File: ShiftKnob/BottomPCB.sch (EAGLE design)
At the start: 38 parts, among them IC2 UA78M05DCY, J1 AVR_SPI_PRG_6PTH, Q1 16MHz, Q2 MOSFET-NCHANNELSMD, Q3 MOSFET-PCHANNELSMD, Q4 MOSFET-NCHANNELSMD, Q5 MOSFET-NCHANNELSMD, Q6 MOSFET-NCHANNELSMD, U1 ATMEGA328, U3 FT232RL-BASICSSOP

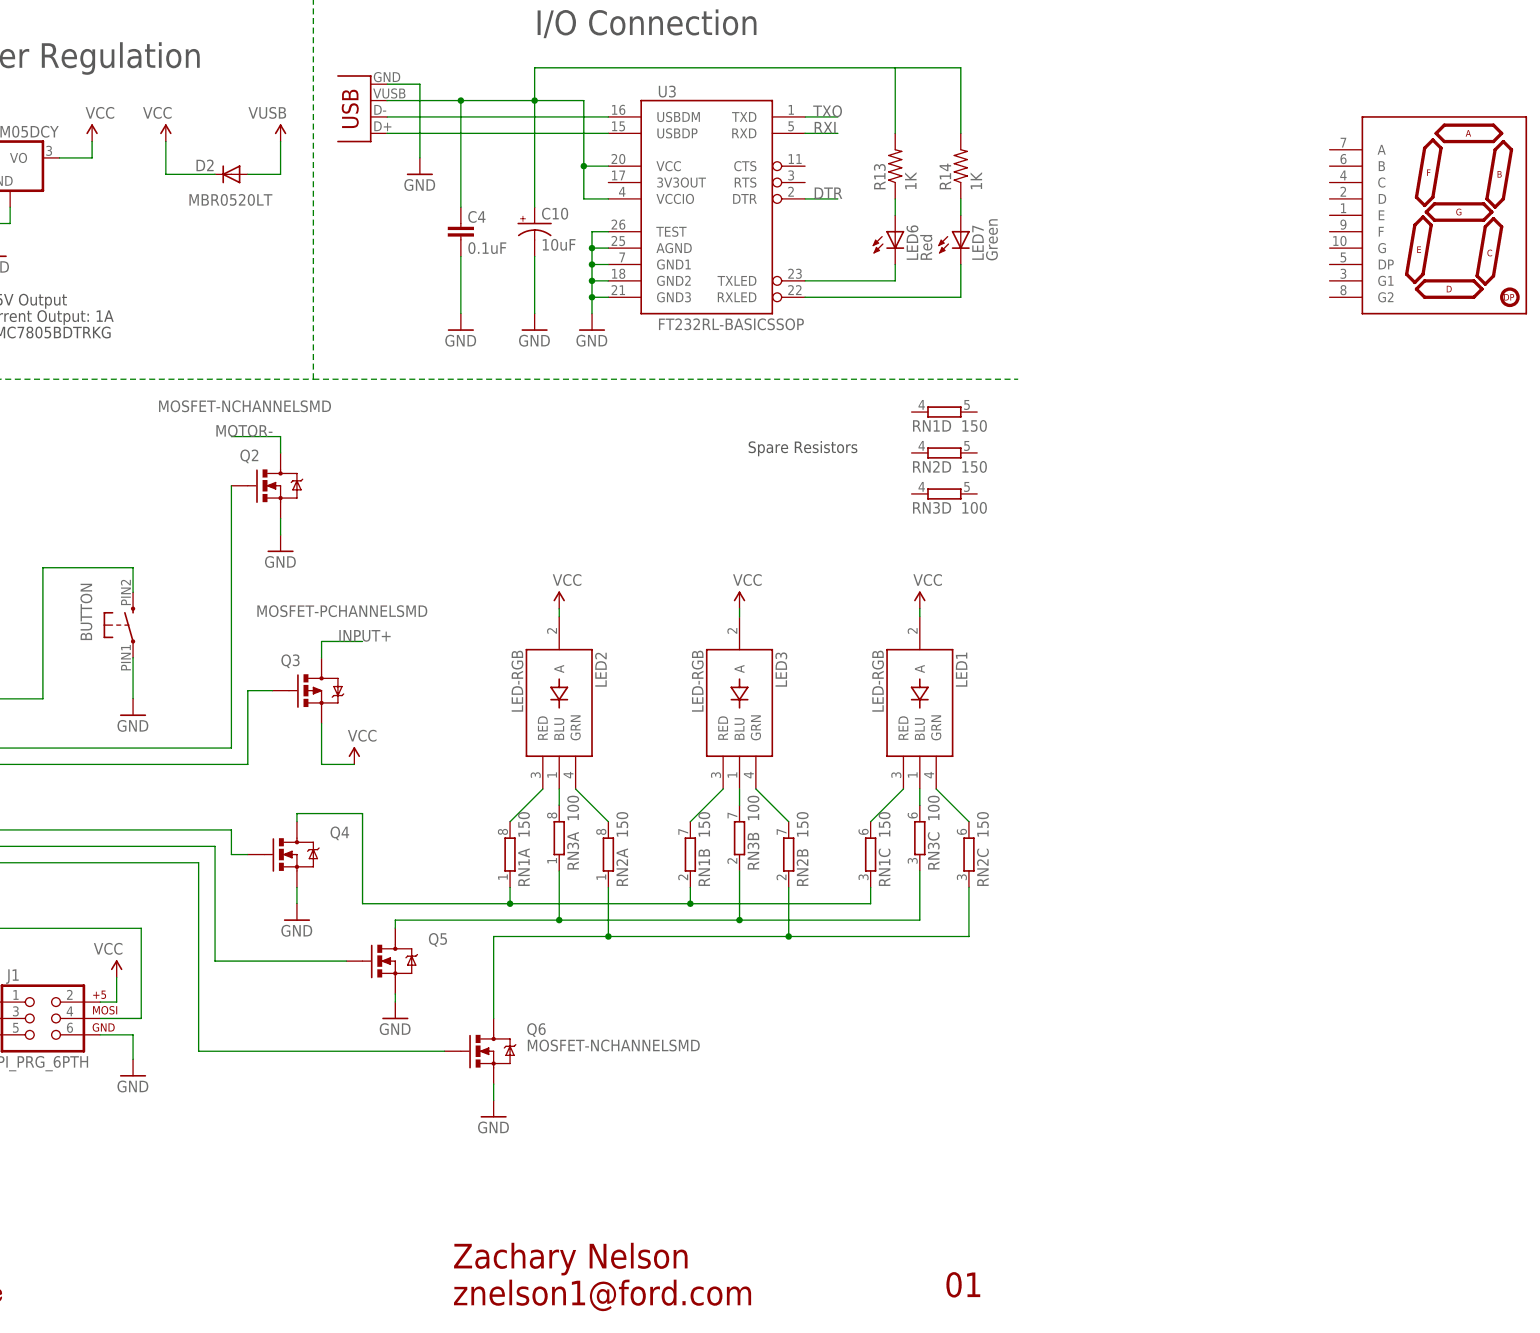
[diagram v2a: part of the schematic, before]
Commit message: swap out button for edge_mount button in Ford_frames library.
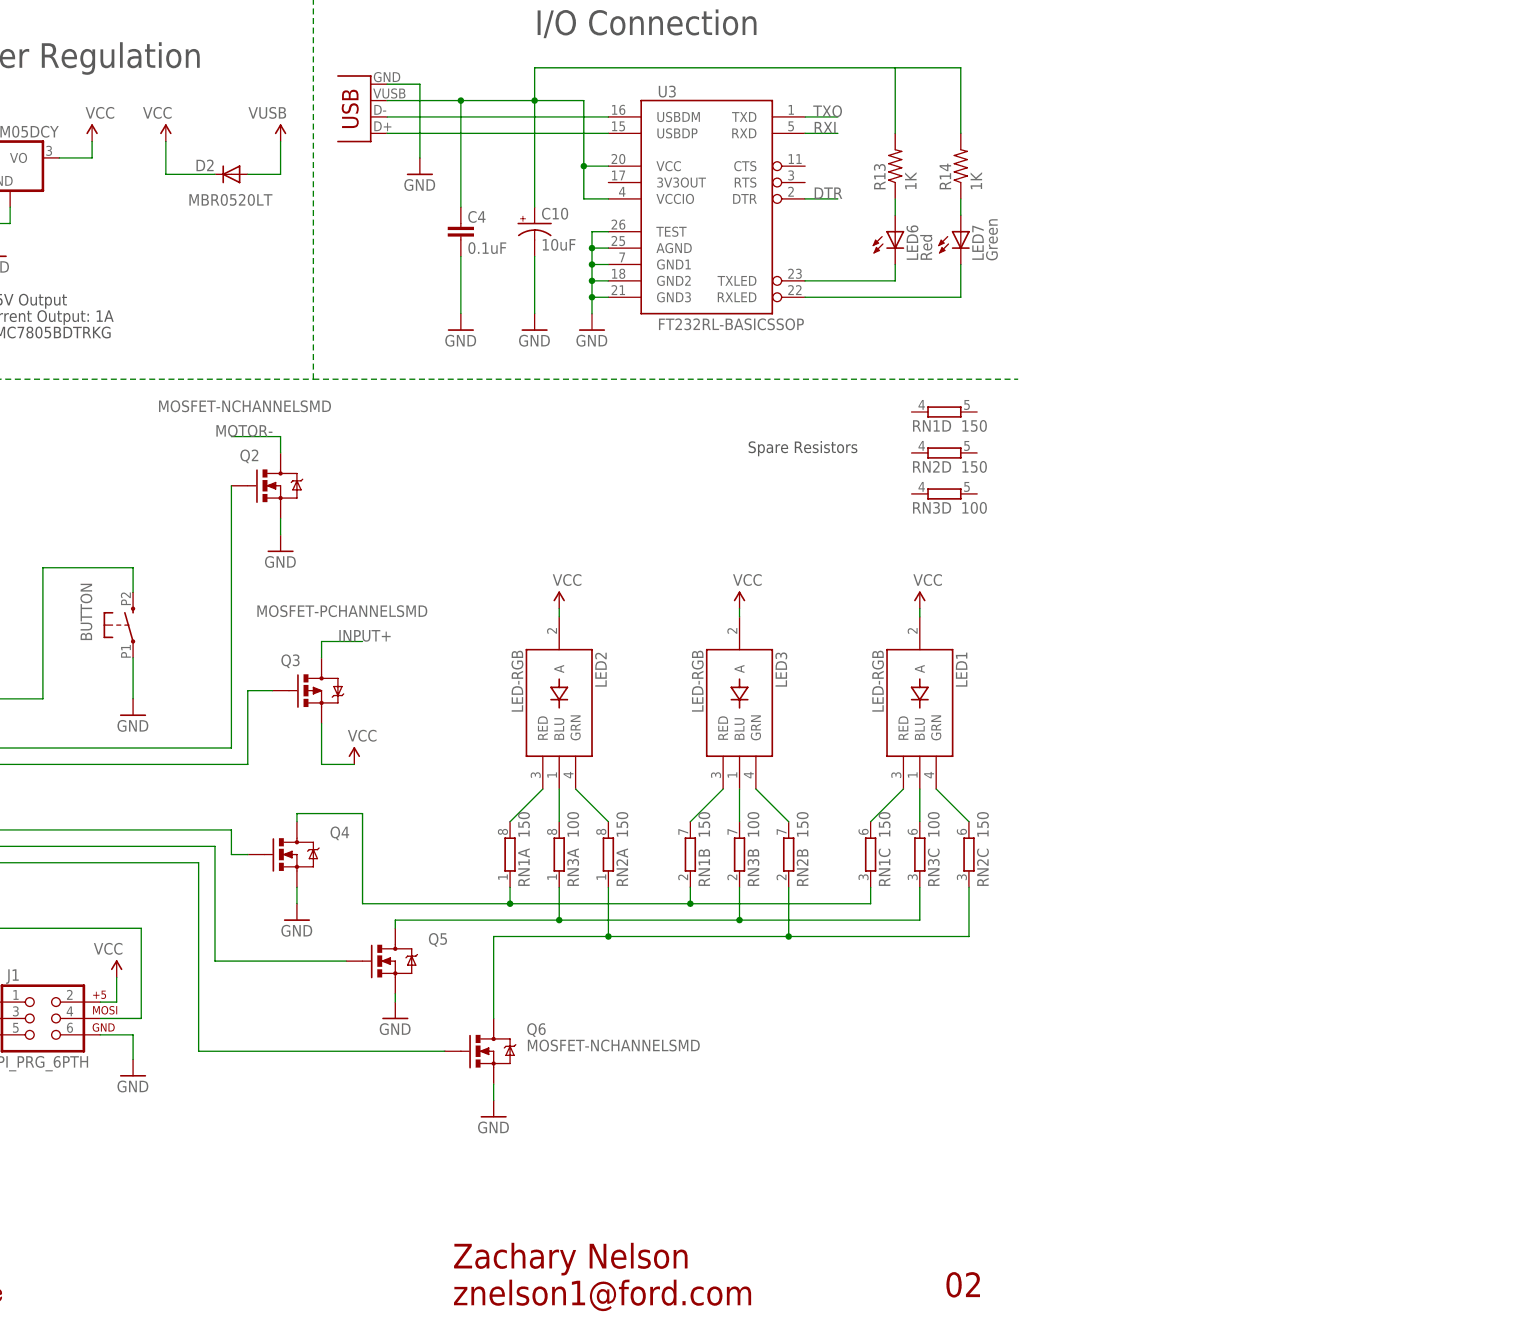
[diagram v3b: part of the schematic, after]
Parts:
- removed U$2: 7-SEGMENT-DISPLAY-1"-RED, SparkFun-Displays:7-SEGMENT-DISPLAY-1"-RED
- BUTTON: value BUTTON_RIGHTANGLE_SMD -> BUTTON_EDGE; device FORD_frames:BUTTON_RIGHTANGLE_SMD -> FORD_frames:BUTTON_EDGE
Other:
- note added: "02"
- note removed: "01"
- moved on the sheet: RN3A, RN3B, RN3C
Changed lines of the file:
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@@
 <part name="P+4" library="SparkFun" deviceset="3.3V" device="" value="VCC"/>
 <part name="P+5" library="SparkFun" deviceset="3.3V" device="" value="VCC"/>
-<part name="BUTTON" library="FORD_frames" deviceset="BUTTON_RIGHTANGLE_SMD" device=""/>
-<part name="U$2" library="SparkFun-Displays" deviceset="7-SEGMENT-DISPLAY-1&quot;-RED" device=""/>
+<part name="BUTTON" library="FORD_frames" deviceset="BUTTON_EDGE" device=""/>
 <part name="UPPER" library="SparkFun-Connectors" deviceset="M04" device="PTH"/>
 <part name="LOWER" library="SparkFun-Connectors" deviceset="M04" device="PTH"/>
@@
 <sheet>
 <plain>
-<text x="264.16" y="8.89" size="3.81" layer="94">01</text>
+<text x="264.16" y="8.89" size="3.81" layer="94">02</text>
 <text x="187.96" y="7.62" size="3.81" layer="94">Zachary Nelson
 znelson1@ford.com</text>
@@
 <instance part="RN2" gate="C" x="267.97" y="77.47" rot="R90"/>
 <instance part="RN2" gate="D" x="264.16" y="139.7"/>
-<instance part="RN3" gate="A" x="204.47" y="80.01" rot="R90"/>
-<instance part="RN3" gate="B" x="232.41" y="80.01" rot="R90"/>
-<instance part="RN3" gate="C" x="260.35" y="80.01" rot="R90"/>
+<instance part="RN3" gate="A" x="204.47" y="77.47" rot="R90"/>
+<instance part="RN3" gate="B" x="232.41" y="77.47" rot="R90"/>
+<instance part="RN3" gate="C" x="260.35" y="77.47" rot="R90"/>
 <instance part="RN3" gate="D" x="264.16" y="133.35"/>
 <instance part="C4" gate="G$1" x="189.23" y="175.26" smashed="yes" rot="R180">
@@
 <attribute name="NAME" x="132.08" y="110.49" size="1.778" layer="95" rot="R90"/>
 </instance>
-<instance part="U$2" gate="G$1" x="344.17" y="176.53"/>
 <instance part="UPPER" gate="G$1" x="15.24" y="180.34"/>
 <instance part="LOWER" gate="G$1" x="15.24" y="160.02"/>
@@
 <segment>
 <label x="101.6" y="78.74" size="1.778" layer="95"/>
-<wire x1="204.47" y1="67.31" x2="204.47" y2="74.93" width="0.1524" layer="91"/>
+<wire x1="204.47" y1="67.31" x2="204.47" y2="72.39" width="0.1524" layer="91"/>
 <wire x1="204.47" y1="67.31" x2="232.41" y2="67.31" width="0.1524" layer="91"/>
-<wire x1="232.41" y1="67.31" x2="232.41" y2="74.93" width="0.1524" layer="91"/>
-<wire x1="260.35" y1="67.31" x2="260.35" y2="74.93" width="0.1524" layer="91"/>
+<wire x1="232.41" y1="67.31" x2="232.41" y2="72.39" width="0.1524" layer="91"/>
+<wire x1="260.35" y1="67.31" x2="260.35" y2="72.39" width="0.1524" layer="91"/>
 <wire x1="232.41" y1="67.31" x2="260.35" y2="67.31" width="0.1524" layer="91"/>
 <junction x="232.41" y="67.31"/>
@@
 <segment>
 <pinref part="LED3" gate="G$1" pin="BLU"/>
-<wire x1="232.41" y1="85.09" x2="232.41" y2="87.63" width="0.1524" layer="91"/>
+<wire x1="232.41" y1="82.55" x2="232.41" y2="87.63" width="0.1524" layer="91"/>
 <pinref part="RN3" gate="B" pin="2"/>
 </segment>
@@
 <segment>
 <pinref part="LED2" gate="G$1" pin="BLU"/>
-<wire x1="204.47" y1="87.63" x2="204.47" y2="85.09" width="0.1524" layer="91"/>
+<wire x1="204.47" y1="87.63" x2="204.47" y2="82.55" width="0.1524" layer="91"/>
 <pinref part="RN3" gate="A" pin="2"/>
 </segment>
@@
 <segment>
 <pinref part="LED1" gate="G$1" pin="BLU"/>
-<wire x1="260.35" y1="85.09" x2="260.35" y2="87.63" width="0.1524" layer="91"/>
+<wire x1="260.35" y1="82.55" x2="260.35" y2="87.63" width="0.1524" layer="91"/>
 <pinref part="RN3" gate="C" pin="2"/>
 </segment>

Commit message: everything on the board. need to route traces.
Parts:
- R13, R14: value 1K -> 10K
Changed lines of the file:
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@@
 <part name="U$6" library="FORD_frames" deviceset="USB-MINI-B_VERTICAL" device=""/>
 <part name="GND20" library="SparkFun" deviceset="GND" device=""/>
-<part name="R13" library="SparkFun" deviceset="RESISTOR" device="0402-RES" value="1K"/>
-<part name="R14" library="SparkFun" deviceset="RESISTOR" device="0402-RES" value="1K"/>
+<part name="R13" library="SparkFun" deviceset="RESISTOR" device="0402-RES" value="10K"/>
+<part name="R14" library="SparkFun" deviceset="RESISTOR" device="0402-RES" value="10K"/>
 <part name="LED6" library="SparkFun" deviceset="LED" device="0603" value="Red"/>
 <part name="LED7" library="SparkFun" deviceset="LED" device="0603" value="Green"/>

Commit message: fix VCC connection on RGB LEDs. Connection was not previously made between pin2 and VCC on each LED.
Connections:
- removed net 3.3V: LED1.A, LED2.A, LED3.A
- net VCC: now also LED1.A, LED2.A, LED3.A
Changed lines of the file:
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@@
 <label x="25.4" y="185.42" size="1.778" layer="95"/>
+</segment>
+<segment>
+<pinref part="LED2" gate="G$1" pin="A"/>
+<wire x1="204.47" y1="115.57" x2="204.47" y2="114.3" width="0.1524" layer="91"/>
+<pinref part="P+3" gate="G$1" pin="3.3V"/>
+</segment>
+<segment>
+<pinref part="LED3" gate="G$1" pin="A"/>
+<wire x1="232.41" y1="115.57" x2="232.41" y2="114.3" width="0.1524" layer="91"/>
+<pinref part="P+4" gate="G$1" pin="3.3V"/>
+</segment>
+<segment>
+<pinref part="LED1" gate="G$1" pin="A"/>
+<wire x1="260.35" y1="115.57" x2="260.35" y2="114.3" width="0.1524" layer="91"/>
+<pinref part="P+5" gate="G$1" pin="3.3V"/>
 </segment>
 </net>
@@
 </segment>
 </net>
-<net name="3.3V" class="0">
-<segment>
-<pinref part="LED2" gate="G$1" pin="A"/>
-<wire x1="204.47" y1="115.57" x2="204.47" y2="114.3" width="0.1524" layer="91"/>
-<pinref part="P+3" gate="G$1" pin="3.3V"/>
-</segment>
-<segment>
-<pinref part="LED3" gate="G$1" pin="A"/>
-<wire x1="232.41" y1="115.57" x2="232.41" y2="114.3" width="0.1524" layer="91"/>
-<pinref part="P+4" gate="G$1" pin="3.3V"/>
-</segment>
-<segment>
-<pinref part="LED1" gate="G$1" pin="A"/>
-<wire x1="260.35" y1="115.57" x2="260.35" y2="114.3" width="0.1524" layer="91"/>
-<pinref part="P+5" gate="G$1" pin="3.3V"/>
-</segment>
-</net>

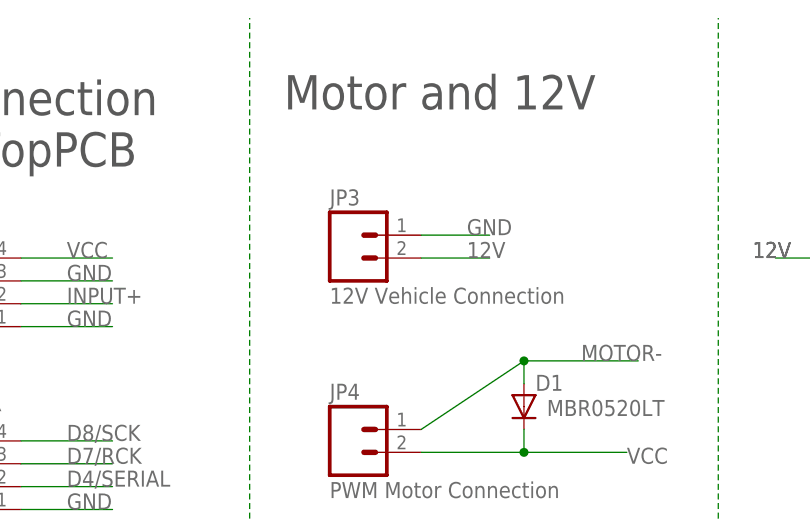
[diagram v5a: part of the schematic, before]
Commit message: change 12V connection to 2 through hole solder points.
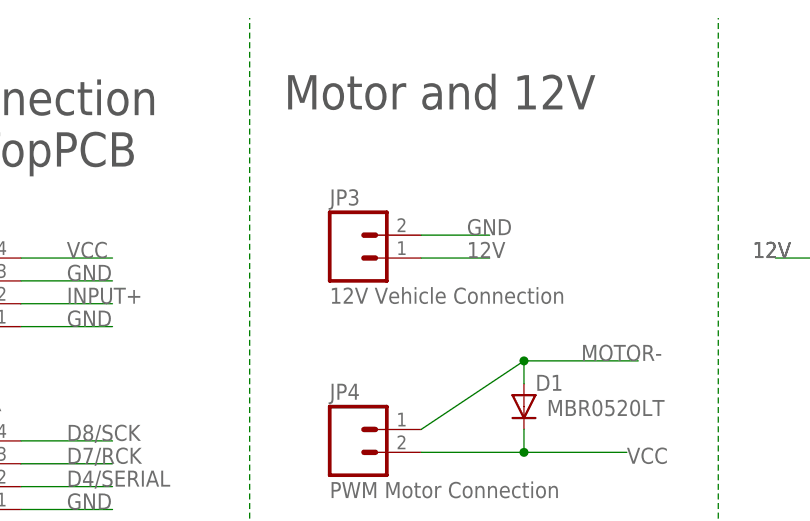
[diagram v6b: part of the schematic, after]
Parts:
- JP3: device SparkFun-Connectors:M02-JST-2MM-SMT -> SparkFun-Connectors:M02PTH; PROD_ID CONN-08352 -> (none)
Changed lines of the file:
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@@
 <part name="C2" library="SparkFun" deviceset="CAP" device="0402-CAP" value="0.1uF"/>
 <part name="U$3" library="SparkFun" deviceset="OSHW-LOGO" device="S"/>
-<part name="JP3" library="SparkFun-Connectors" deviceset="M02" device="-JST-2MM-SMT" value="12V Vehicle Connection">
-<attribute name="PROD_ID" value="CONN-08352"/>
-</part>
+<part name="JP3" library="SparkFun-Connectors" deviceset="M02" device="PTH" value="12V Vehicle Connection"/>
 <part name="LED2" library="FORD_frames" deviceset="LED-RGB" device=""/>
 <part name="LED3" library="FORD_frames" deviceset="LED-RGB" device=""/>

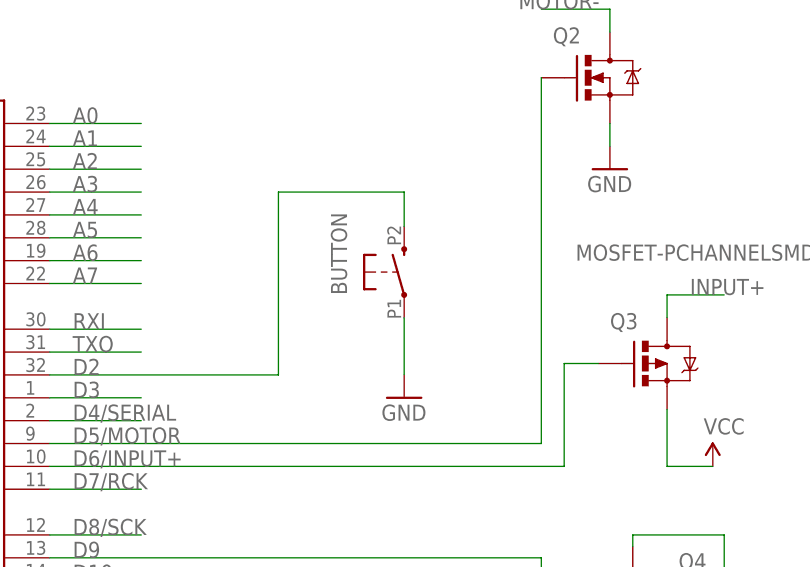
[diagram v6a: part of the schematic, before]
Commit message: swap pins on button for easier board layout.
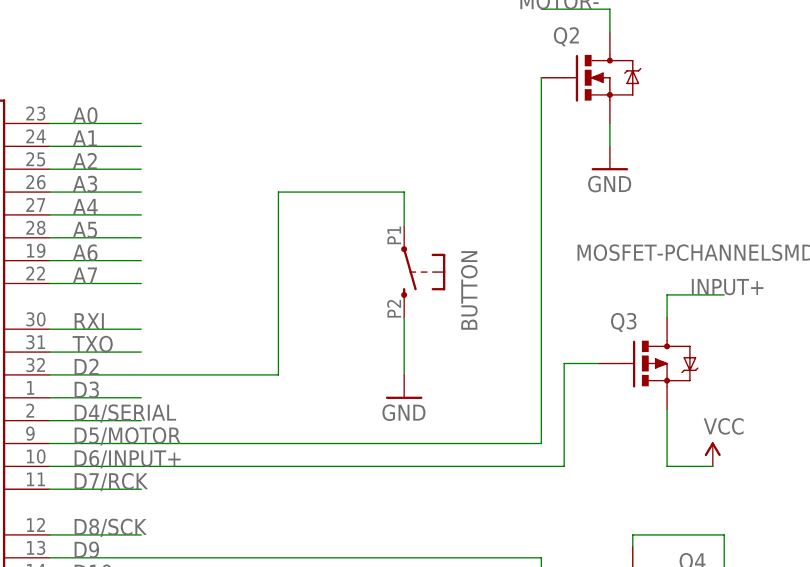
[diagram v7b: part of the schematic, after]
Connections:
- net D2: now also BUTTON.1; no longer BUTTON.2
- net GND: now also BUTTON.2; no longer BUTTON.1
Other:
- moved on the sheet: BUTTON
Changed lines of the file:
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@@
 <setting verticaltext="up"/>
 </settings>
-<grid distance="0.1" unitdist="inch" unit="inch" style="lines" multiple="1" display="no" altdistance="0.01" altunitdist="inch" altunit="inch"/>
+<grid distance="0.05" unitdist="inch" unit="inch" style="lines" multiple="1" display="no" altdistance="0.01" altunitdist="inch" altunit="inch"/>
 <layers>
 <layer number="1" name="Top" color="4" fill="1" visible="no" active="no"/>
@@
 <instance part="P+4" gate="G$1" x="232.41" y="115.57"/>
 <instance part="P+5" gate="G$1" x="260.35" y="115.57"/>
-<instance part="BUTTON" gate="G$1" x="138.43" y="113.03" smashed="yes" rot="R90">
-<attribute name="NAME" x="132.08" y="110.49" size="1.778" layer="95" rot="R90"/>
+<instance part="BUTTON" gate="G$1" x="138.43" y="113.03" smashed="yes" rot="R270">
+<attribute name="NAME" x="144.78" y="115.57" size="1.778" layer="95" rot="R270"/>
 </instance>
 <instance part="UPPER" gate="G$1" x="15.24" y="180.34"/>
@@
 </net>
 <net name="GND" class="0">
-<segment>
-<wire x1="138.43" y1="107.95" x2="138.43" y2="101.6" width="0.1524" layer="91"/>
-<pinref part="GND3" gate="1" pin="GND"/>
-<pinref part="BUTTON" gate="G$1" pin="1"/>
-</segment>
 <segment>
 <wire x1="33.02" y1="49.53" x2="33.02" y2="52.07" width="0.1524" layer="91"/>
@@
 <label x="25.4" y="157.48" size="1.778" layer="95"/>
 </segment>
+<segment>
+<pinref part="GND3" gate="1" pin="GND"/>
+<pinref part="BUTTON" gate="G$1" pin="2"/>
+<wire x1="138.43" y1="101.6" x2="138.43" y2="107.95" width="0.1524" layer="91"/>
+</segment>
 </net>
 <net name="VCC" class="0">
@@
 <segment>
 <label x="101.6" y="101.6" size="1.778" layer="95"/>
-<wire x1="138.43" y1="121.92" x2="138.43" y2="118.11" width="0.1524" layer="91"/>
 <pinref part="U1" gate="G$1" pin="PD2(INT0)"/>
 <wire x1="99.06" y1="101.6" x2="124.46" y2="101.6" width="0.1524" layer="91"/>
 <wire x1="124.46" y1="101.6" x2="124.46" y2="121.92" width="0.1524" layer="91"/>
 <wire x1="124.46" y1="121.92" x2="138.43" y2="121.92" width="0.1524" layer="91"/>
-<pinref part="BUTTON" gate="G$1" pin="2"/>
-</segment>
-</net>
+<pinref part="BUTTON" gate="G$1" pin="1"/>
+<wire x1="138.43" y1="118.11" x2="138.43" y2="121.92" width="0.1524" layer="91"/>
+</segment>
+</net>
